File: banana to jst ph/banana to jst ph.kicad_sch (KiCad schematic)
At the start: 12 parts, among them J1 USB4125-GF-A-0190, J2 Positive, J3 Negative

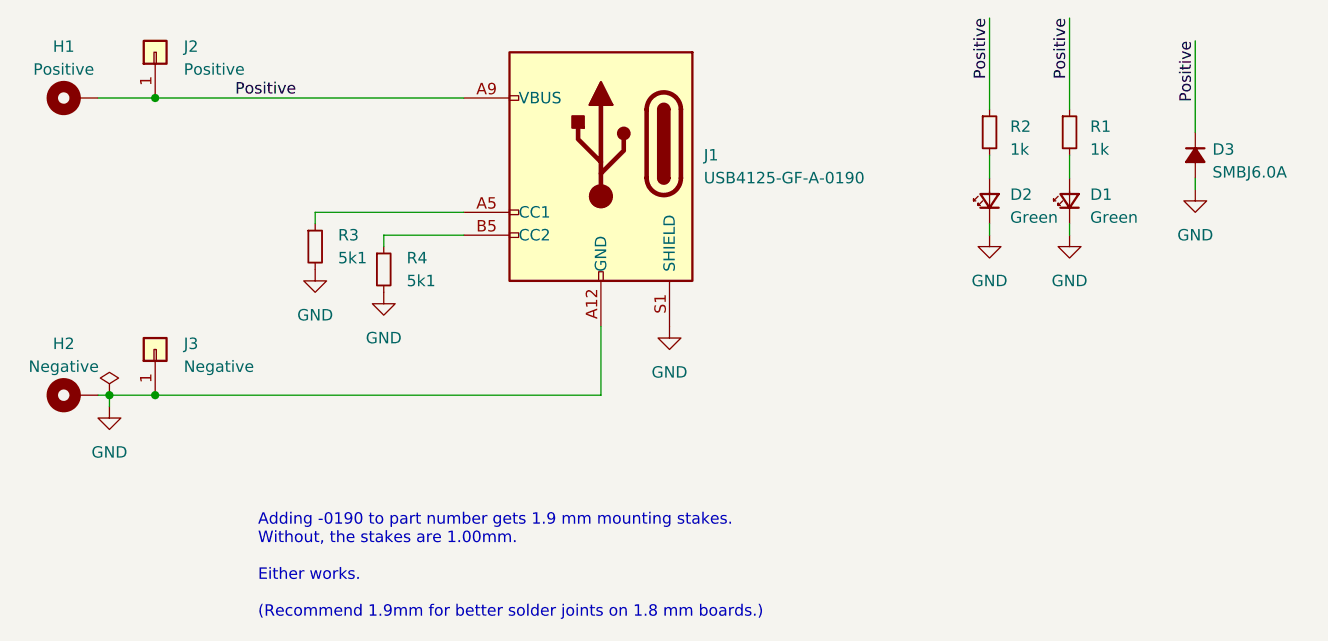
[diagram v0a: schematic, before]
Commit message: updated schematic but need to verify pin 1 and 2 connections
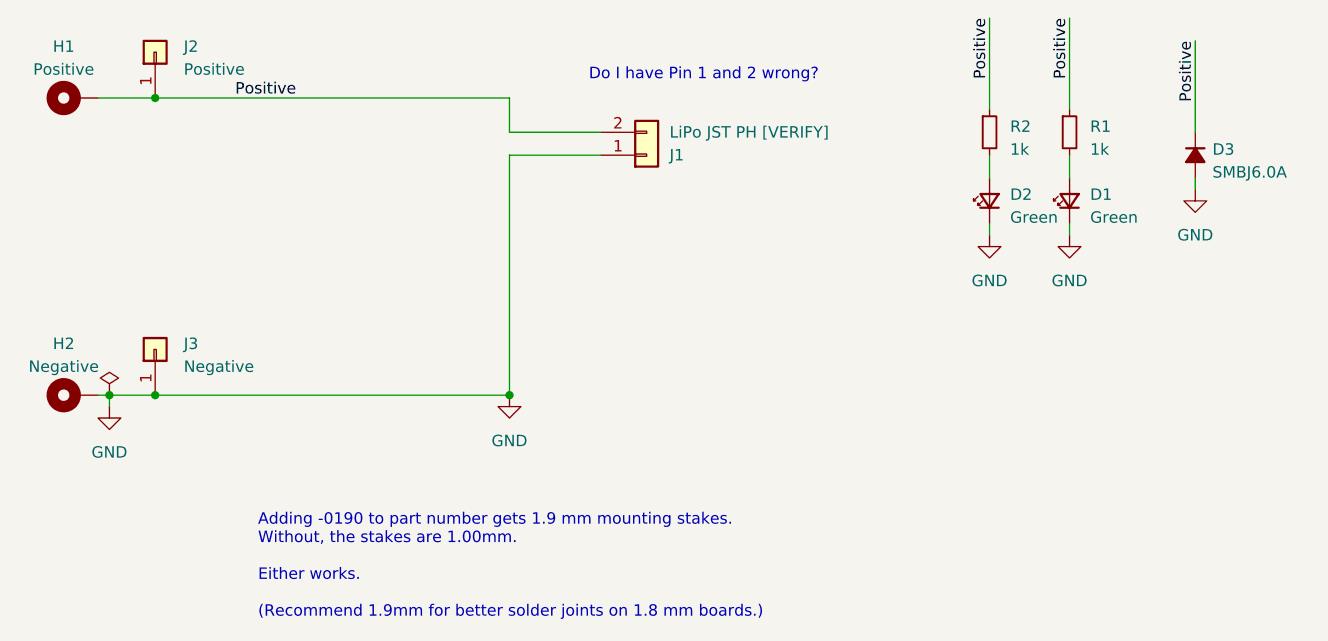
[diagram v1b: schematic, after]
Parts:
- removed J1: USB4125-GF-A-0190, Connector_USB:USB_C_Receptacle_GCT_USB4125-xx-x_6P_TopMnt_Horizontal, symbol Connector:USB_C_Receptacle_PowerOnly_6P
- removed R3, R4: 5k1, Resistor_SMD:R_1206_3216Metric_Pad1.30x1.75mm_HandSolder, symbol Device:R_Small
- added J1: LiPo JST PH [VERIFY], Connector_JST:JST_PH_S2B-PH-K_1x02_P2.00mm_Horizontal, symbol Connector_Generic:Conn_01x02
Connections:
- net GND: now also J1.1 (Pin_1)
- net Positive: now also J1.2 (Pin_2)
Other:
- note added: "Do I have Pin 1 and 2 wrong?"
- title: Banana to USB-C Adapter (Power Only) -> Banana to JST PH (LiPo)

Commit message: jst ph sm4 adapter rev 2 ready for fab
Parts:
- J1: value LiPo JST PH [VERIFY] -> JST S2B-PH-SM4; footprint Connector_JST:JST_PH_S2B-PH-K_1x02_P2.00mm_Horizontal -> Connector_JST:JST_PH_S2B-PH-SM4-TB_1x02-1MP_P2.00mm_Horizontal
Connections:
- net GND: now also J1.2 (Pin_2); no longer J1.1 (Pin_1)
- net Positive: now also J1.1 (Pin_1); no longer J1.2 (Pin_2)
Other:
- note removed: "Do I have Pin 1 and 2 wrong?"
- title: Banana to JST PH (LiPo) -> Banana to JST PH SM4 (LiPo)
- moved on the sheet: H1, H2, J2, J3

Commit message: added SPN for JST
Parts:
- J1: Newark (none) -> 38K8067
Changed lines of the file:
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@@
+			)
+		)
+		(property "Newark" "38K8067"
+			(at 133.35 95.25 0)
+			(effects
+				(font
+					(size 1.27 1.27)
+				)
+				(hide yes)
 			)
 		)
